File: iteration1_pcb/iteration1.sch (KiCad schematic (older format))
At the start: 0 parts

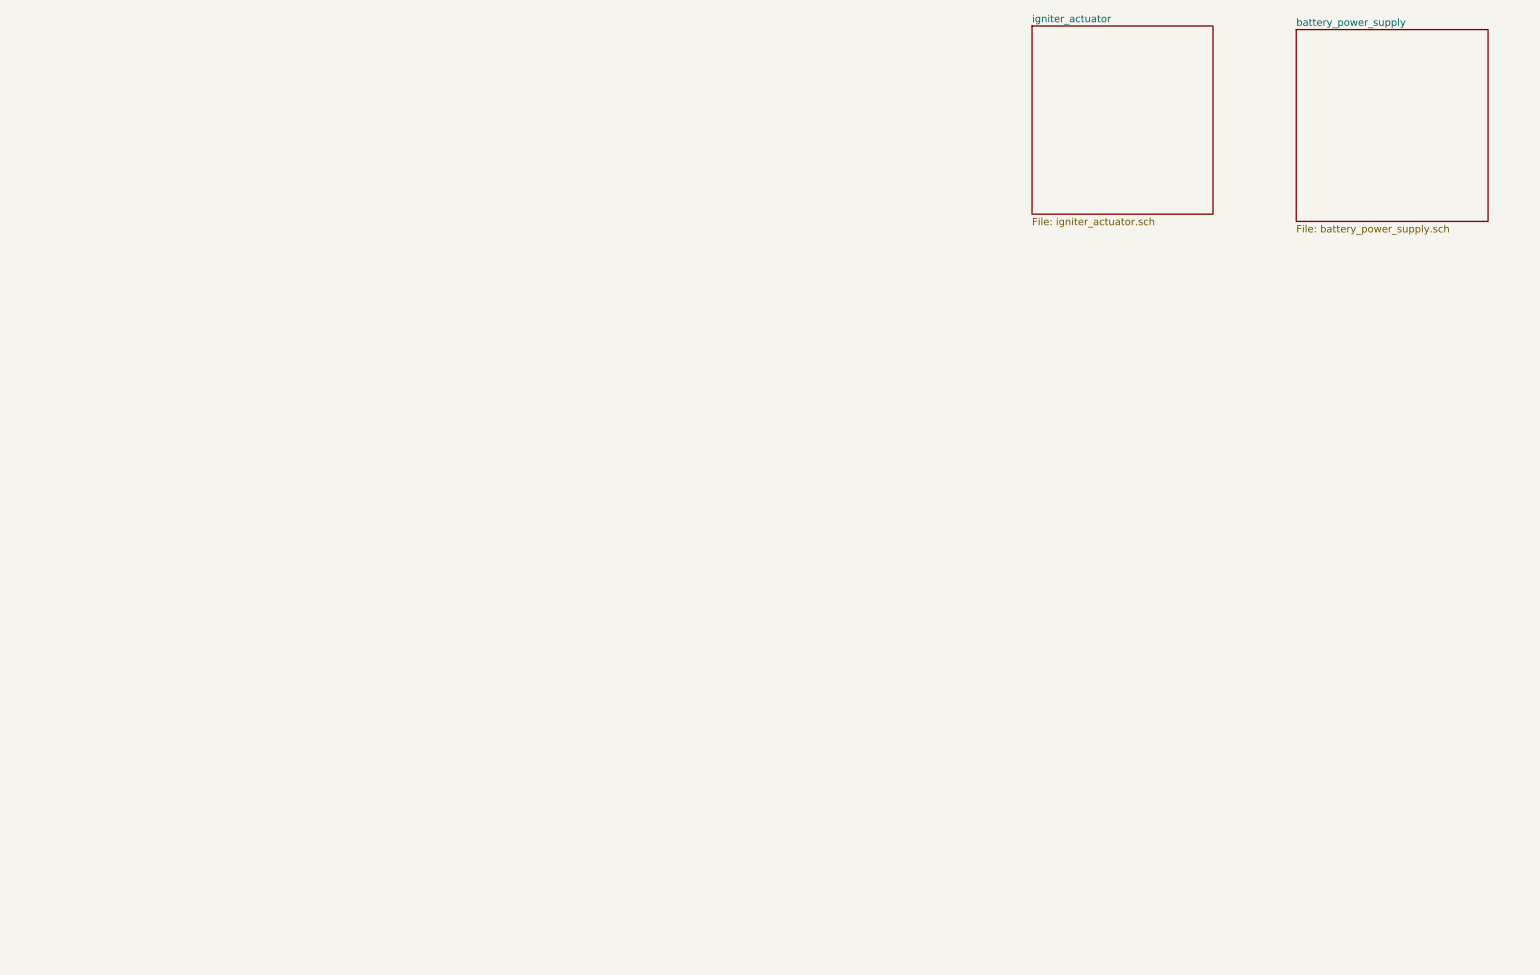
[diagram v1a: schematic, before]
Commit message: Adding schematic work
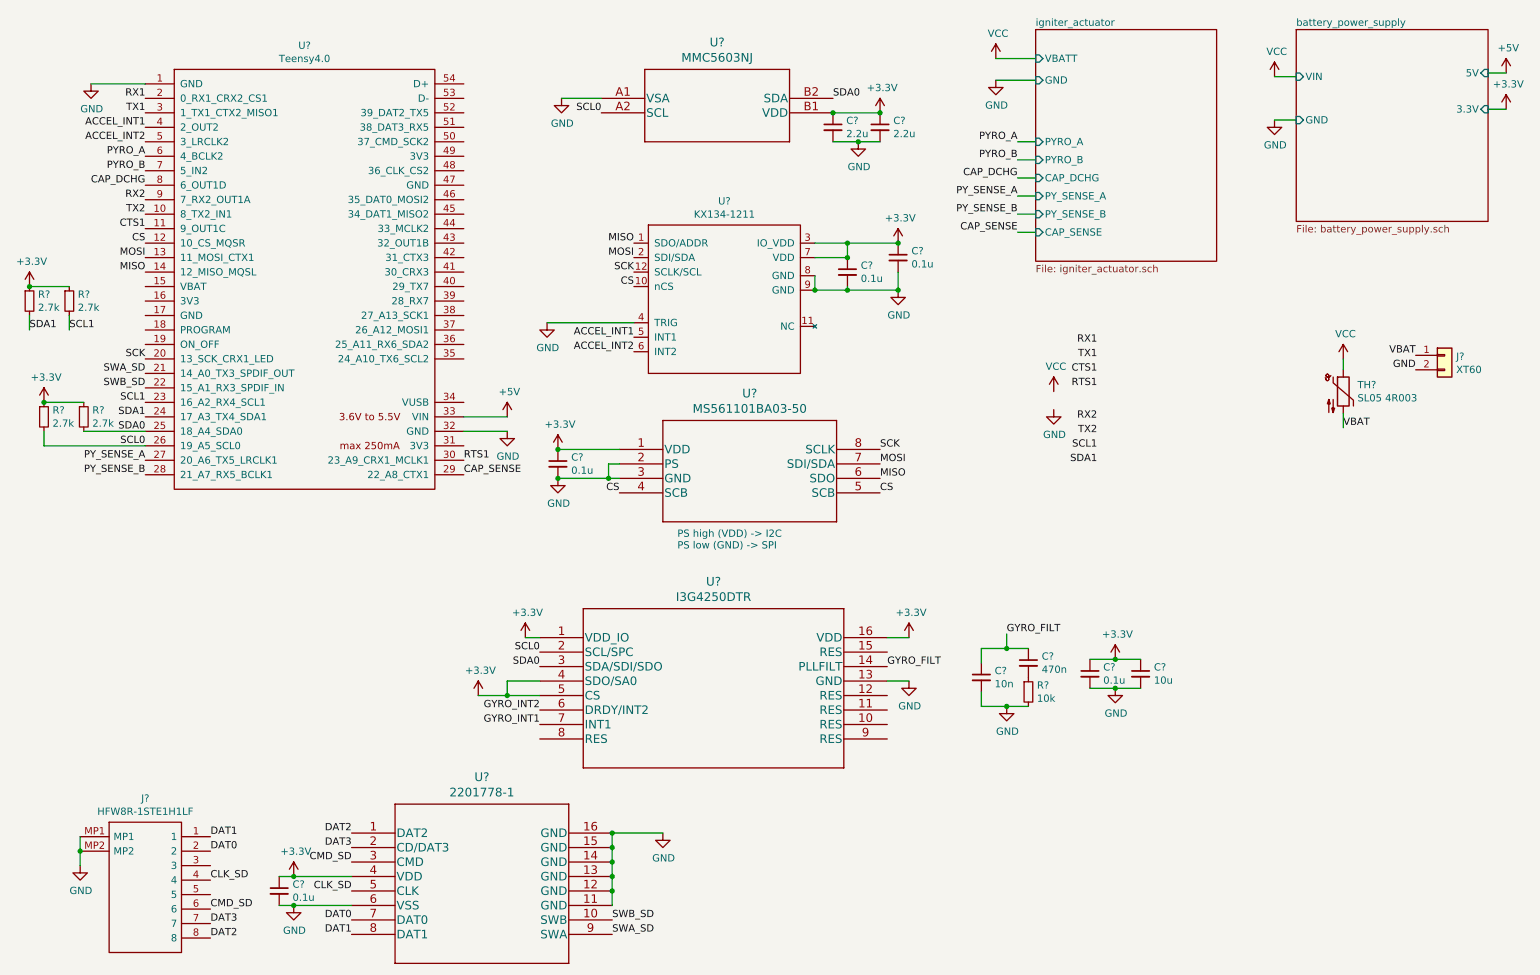
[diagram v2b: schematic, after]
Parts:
- added C? (x5): 0.1u, symbol Device:C_Small
- added C?: 10u, symbol Device:C_Small
- added C? (x2): 2.2u, symbol Device:C_Small
- added C?: 10n, symbol Device:C_Small
- added C?: 470n, symbol Device:C_Small
- added J?: HFW8R-1STE1H1LF, HFW8R1STE1H1LF, symbol symbols:HFW8R-1STE1H1LF
- added J?: XT60, symbol Connector_Generic:Conn_01x02
- added R? (x4): 2.7k, symbol Device:R_Small
- added R?: 10k, symbol Device:R_Small
- added TH?: SL05 4R003, symbol Device:Thermistor_NTC
- added U?: Teensy4.0, symbol teensy:Teensy4.0
- added U?: MMC5603NJ, WLP4_0P82X0P82_MEM, symbol symbols:MMC5603NJ
- added U?: MS561101BA03-50, SON8_MS5611_TEC, symbol symbols:MS561101BA03-50
- added U?: KX134-1211, symbol symbols:KX134-1211
- added U?: I3G4250DTR, LGA-16_4X4X1_STM, symbol symbols:I3G4250DTR
- added U?: 2201778-1, 2201778-1_TEC, symbol symbols:2201778-1
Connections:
- new net: C?.2, R?.1
- new net +3V3: C?.1, C?.1, C?.1, C?.1, C?.1, C?.1, C?.1, C?.1, R?.1, R?.1, R?.1, R?.1, U?.1 (VDD), U?.1 (VDD_IO), U?.16 (VDD), U?.3 (IO_VDD), U?.4 (SDO/SA0), U?.4 (VDD), U?.5 (CS), U?.7 (VDD), U?.B1 (VDD)
- new net +5V: U?.33 (VIN)
- new net ACCEL_INT1: U?.4 (2_OUT2), U?.5 (INT1)
- new net ACCEL_INT2: U?.5 (3_LRCLK2), U?.6 (INT2)
- new net CAP_DCHG: U?.8 (6_OUT1D)
- new net CAP_SENSE: U?.29 (22_A8_CTX1)
- new net CLK_SD: J?.4, U?.5 (CLK)
- new net CMD_SD: J?.6, U?.3 (CMD)
- new net CS: U?.10 (nCS), U?.12 (10_CS_MQSR), U?.4 (SCB), U?.5 (SCB)
- new net CTS1: U?.11 (9_OUT1C)
- new net DAT0: J?.2, U?.7 (DAT0)
- new net DAT1: J?.1, U?.8 (DAT1)
- new net DAT2: J?.8, U?.1 (DAT2)
- new net DAT3: J?.7, U?.2 (CD/DAT3)
- new net GND: C?.2, C?.2, C?.2, C?.2, C?.2, C?.2, C?.2, C?.2, C?.2, J?.2 (Pin_2), J?.MP1, J?.MP2, R?.2, U?.1 (GND), U?.11 (GND), U?.12 (GND), U?.13 (GND), U?.13 (GND), U?.14 (GND), U?.15 (GND), U?.16 (GND), U?.2 (PS), U?.3 (GND), U?.32 (GND), U?.4 (TRIG), U?.6 (VSS), U?.8 (GND), U?.9 (GND), U?.A1 (VSA)
- new net GYRO_FILT: C?.1, C?.1, U?.14 (PLLFILT)
- new net GYRO_INT1: U?.7 (INT1)
- new net GYRO_INT2: U?.6 (DRDY/INT2)
- new net MISO: U?.1 (SDO/ADDR), U?.14 (12_MISO_MQSL), U?.6 (SDO)
- new net MOSI: U?.13 (11_MOSI_CTX1), U?.2 (SDI/SDA), U?.7 (SDI/SDA)
- new net PYRO_A: U?.6 (4_BCLK2)
- new net PYRO_B: U?.7 (5_IN2)
- new net PY_SENSE_A: U?.27 (20_A6_TX5_LRCLK1)
- new net PY_SENSE_B: U?.28 (21_A7_RX5_BCLK1)
- new net RTS1: U?.30 (23_A9_CRX1_MCLK1)
- new net RX1: U?.2 (0_RX1_CRX2_CS1)
- new net RX2: U?.9 (7_RX2_OUT1A)
- new net SCK: U?.12 (SCLK/SCL), U?.20 (13_SCK_CRX1_LED), U?.8 (SCLK)
- new net SCL0: R?.2, U?.2 (SCL/SPC), U?.26 (19_A5_SCL0), U?.A2 (SCL)
- new net SCL1: R?.2, U?.23 (16_A2_RX4_SCL1)
- new net SDA0: R?.2, U?.25 (18_A4_SDA0), U?.3 (SDA/SDI/SDO), U?.B2 (SDA)
- new net SDA1: R?.2, U?.24 (17_A3_TX4_SDA1)
- new net SWA_SD: U?.21 (14_A0_TX3_SPDIF_OUT), U?.9 (SWA)
- new net SWB_SD: U?.10 (SWB), U?.22 (15_A1_RX3_SPDIF_IN)
- new net TX1: U?.3 (1_TX1_CTX2_MISO1)
- new net TX2: U?.10 (8_TX2_IN1)
- new net VBAT: J?.1 (Pin_1), TH?.2
- new net VCC: TH?.1
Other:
- note added: "PS high (VDD) -> I2C\nPS low (GND) -> SPI"
